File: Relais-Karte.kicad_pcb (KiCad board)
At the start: 2 copper layers, 38.5 x 74.5 mm, 18 parts, among them J1 MKDS_3-2_5.08, J2 MKDS_3-2_5.08, J3 MKDS_3-3_5.08, J4 MKDS_3-2_5.08, K1 G2RL-1-E, Q1 BC846, Q2 BC846, SW1 L101011MS02Q, U1 TL431DBZ, U2 TL431DBZ

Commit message: wip
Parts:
- added PCB1: ~, _PS_LIB_PCB:_PCB, F.Cu at (130.1, 85.0)
- added Repo1: ~, _PS_LIB_PCB:_Repository, B.Cu at (129.0, 92.9)
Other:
- board text added: "${COMMENT1}"
- board text added: "${COMMENT2}"
- board text added: "${COMMENT3}"
- board text added: "${COMMENT4}"
- board text added: "${COMPANY}"
- board text added: "${ISSUE_DATE}"
- board text added: "${REVISION}"
- board text added: "${TITLE}"
- board text removed: "Relais-Karte 190326"

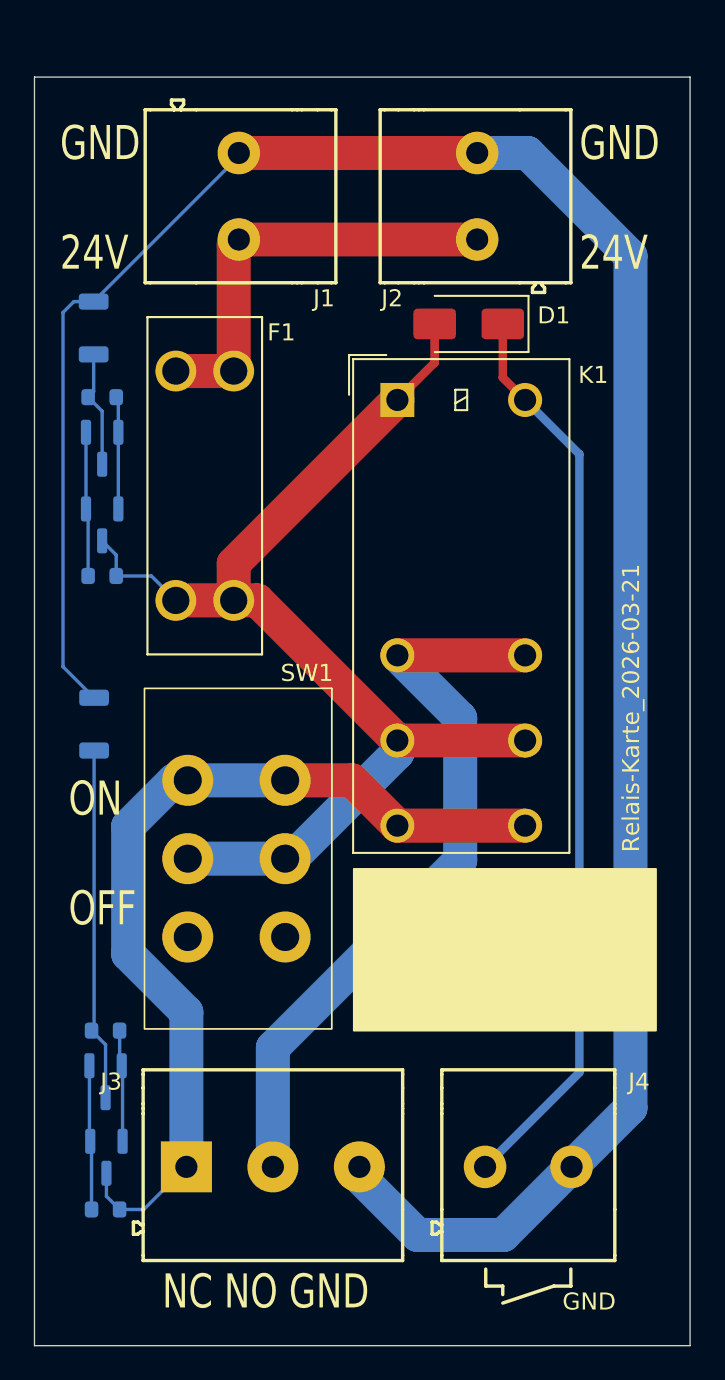
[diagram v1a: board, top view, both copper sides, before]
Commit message: länge der platine angepasst
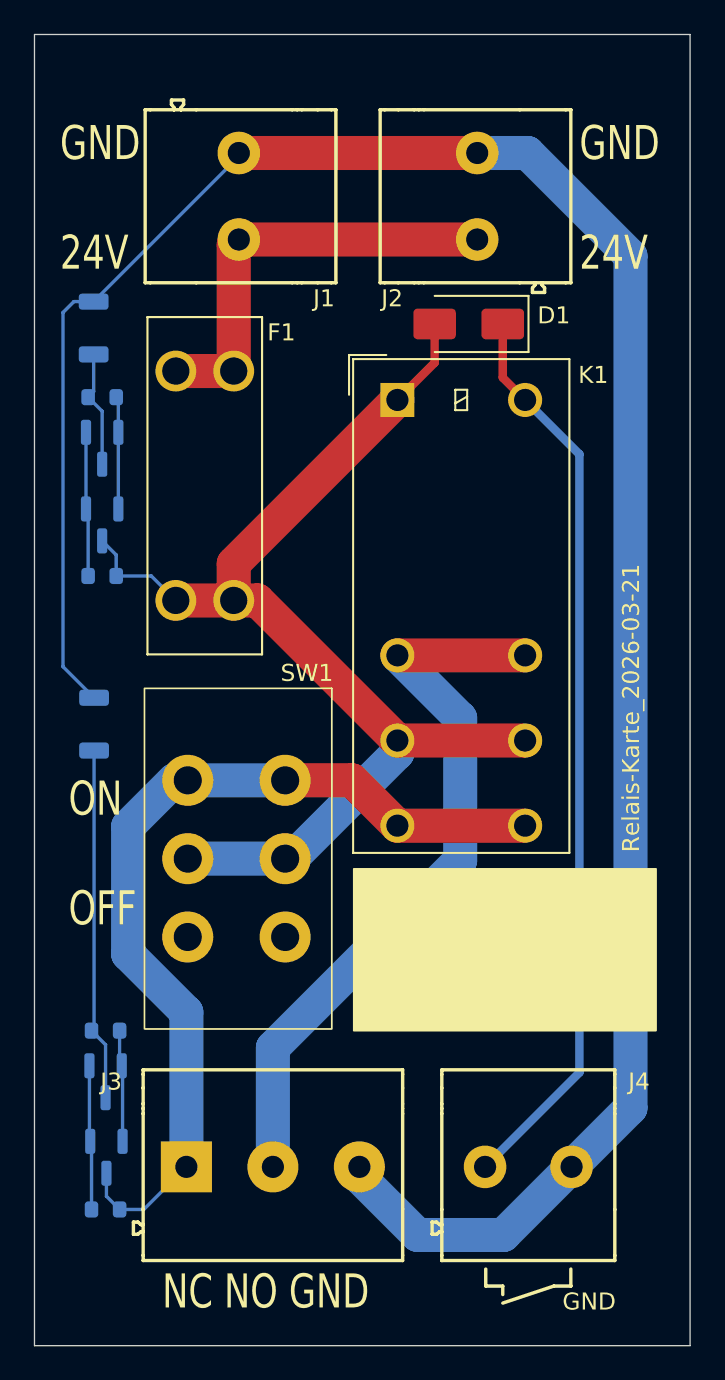
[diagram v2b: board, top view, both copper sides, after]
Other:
- board size 38.5 x 74.5 mm -> 38.5 x 77 mm
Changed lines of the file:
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@@
 	)
 	(gr_rect
-		(start 94.5 39.5)
+		(start 94.5 37)
 		(end 133 114)
 		(stroke
@@
 		(layer "User.1")
 		(pts
-			(xy 94.5 114) (xy 94.5 38.5)
+			(xy 94.5 114) (xy 94.5 37)
 		)
 		(height -3.5)
@@
 			(keep_text_aligned yes)
 		)
-		(gr_text "75,5"
-			(at 89.85 76.25 90)
+		(gr_text "77"
+			(at 89.85 75.5 90)
 			(layer "User.1")
 			(effects
@@
 		(polygon
 			(pts
-				(xy 94.5 114) (xy 133 114) (xy 133 112.5) (xy 96 112.5) (xy 96 41) (xy 131.5 41) (xy 131.5 112.5)
-				(xy 133 112.5) (xy 133 39.5) (xy 94.5 39.5)
+				(xy 94.5 114) (xy 133 114) (xy 133 112.5) (xy 96 112.5) (xy 96 38.5) (xy 131.5 38.5) (xy 131.5 112.5)
+				(xy 133 112.5) (xy 133 37) (xy 94.5 37)
 			)
 		)
